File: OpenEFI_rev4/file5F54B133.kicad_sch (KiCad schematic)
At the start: 104 parts, among them J9 Conn_02x06_Top_Bottom, Q14 AO3400A, Q15 AO3400A, Q16 AO3400A, U10 LMV324, U19 f042_wideband_module, U2 74HC4851, U25 TJA1051T-3, U26 SP720ABTG, U8 BMP280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

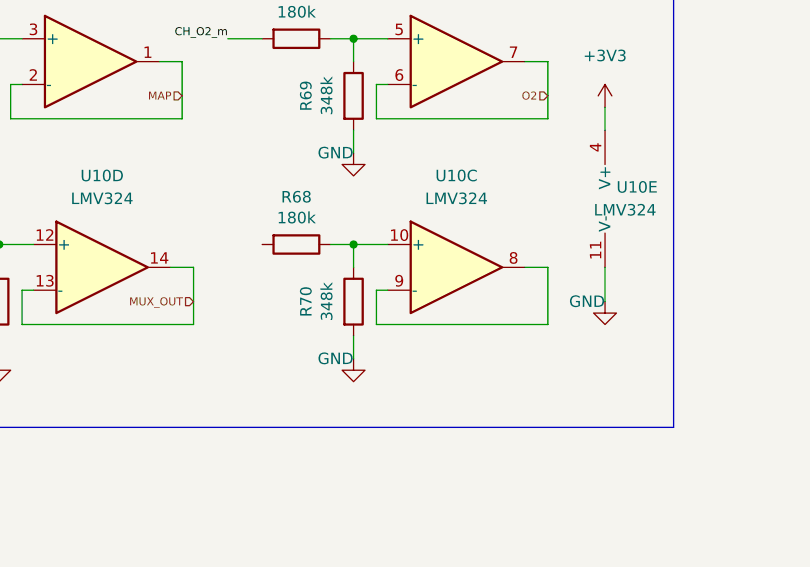
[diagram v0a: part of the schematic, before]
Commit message: update sensors/connector pinout, added rtc vbatt backup
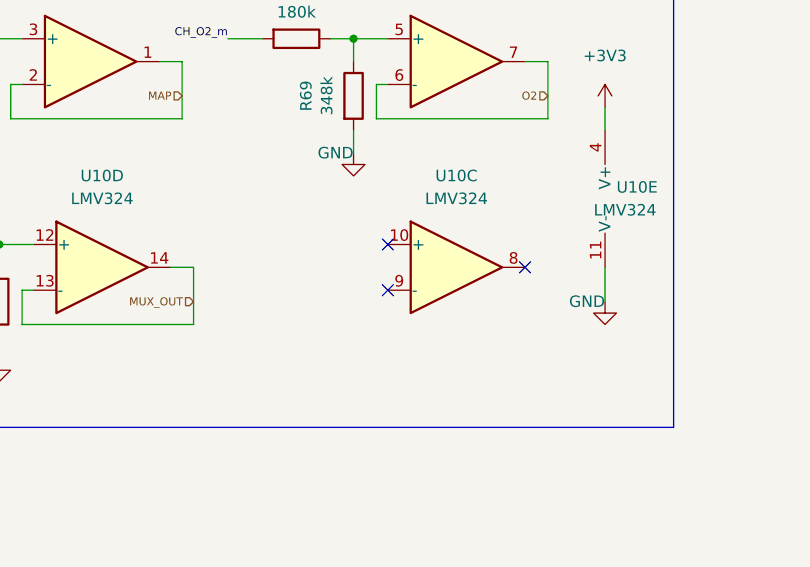
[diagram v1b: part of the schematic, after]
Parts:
- removed R68: 180k, Resistor_SMD:R_0805_2012Metric, symbol Device:R
- removed R70: 348k, Resistor_SMD:R_0805_2012Metric, symbol Device:R
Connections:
- net at U10.8: no longer U10.9 (-)
- no-connect marks 2 -> 5
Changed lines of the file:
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@@
   (junction (at 170.815 90.17) (diameter 0) (color 0 0 0 0)
   )
-  (junction (at 168.91 220.98) (diameter 0) (color 0 0 0 0)
-  )
   (junction (at 74.93 144.78) (diameter 0) (color 0 0 0 0)
   )
@@
   (junction (at 319.405 38.1) (diameter 0) (color 0 0 0 0)
   )
+  (no_connect (at 172.72 226.06))
+  (no_connect (at 172.72 220.98))
   (no_connect (at 300.355 76.2))
   (no_connect (at 313.055 66.04))
+  (no_connect (at 187.96 223.52))
   (wire (pts (xy 171.45 203.2) (xy 171.45 207.01))
     (stroke (width 0) (type default))
@@
     (stroke (width 0) (type default))
   )
-  (wire (pts (xy 171.45 226.06) (xy 171.45 229.87))
-    (stroke (width 0) (type default))
-  )
   (wire (pts (xy 241.3 71.755) (xy 241.3 73.66))
     (stroke (width 0) (type default))
@@
     (stroke (width 0) (type default))
   )
-  (wire (pts (xy 168.91 233.68) (xy 168.91 231.14))
-    (stroke (width 0) (type default))
-  )
   (wire (pts (xy 85.725 223.52) (xy 85.725 226.695))
     (stroke (width 0) (type default))
@@
     (stroke (width 0) (type default))
   )
-  (wire (pts (xy 172.72 226.06) (xy 171.45 226.06))
-    (stroke (width 0) (type default))
-  )
   (polyline (pts (xy 184.785 26.67) (xy 184.785 51.435))
     (stroke (width 0) (type default))
@@
     (stroke (width 0) (type default))
   )
-  (wire (pts (xy 168.91 220.98) (xy 168.91 223.52))
-    (stroke (width 0) (type default))
-  )
   (wire (pts (xy 381 39.37) (xy 390.525 39.37))
     (stroke (width 0) (type default))
@@
     (stroke (width 0) (type default))
   )
-  (wire (pts (xy 190.5 229.87) (xy 190.5 223.52))
-    (stroke (width 0) (type default))
-  )
   (wire (pts (xy 381 41.91) (xy 390.525 41.91))
     (stroke (width 0) (type default))
@@
     (stroke (width 0) (type default))
   )
-  (wire (pts (xy 190.5 223.52) (xy 187.96 223.52))
-    (stroke (width 0) (type default))
-  )
   (wire (pts (xy 114.935 45.72) (xy 118.745 45.72))
     (stroke (width 0) (type default))
@@
     (stroke (width 0) (type default))
   )
-  (wire (pts (xy 168.91 220.98) (xy 172.72 220.98))
-    (stroke (width 0) (type default))
-  )
   (wire (pts (xy 35.56 147.32) (xy 35.56 149.86))
     (stroke (width 0) (type default))
@@
     (stroke (width 0) (type default))
   )
-  (wire (pts (xy 166.37 220.98) (xy 168.91 220.98))
-    (stroke (width 0) (type default))
-  )
   (wire (pts (xy 128.905 48.26) (xy 128.905 45.72))
     (stroke (width 0) (type default))
@@
     (stroke (width 0) (type default))
   )
-  (wire (pts (xy 171.45 229.87) (xy 190.5 229.87))
-    (stroke (width 0) (type default))
-  )
   (polyline (pts (xy 60.96 204.47) (xy 60.96 241.3))
     (stroke (width 0) (type default))
@@
     )
   )
-  (symbol (lib_id "Device:R") (at 162.56 220.98 270) (unit 1)
-    (in_bom yes) (on_board yes) (dnp no)
-    (property "Reference" "R68" (at 162.56 215.7222 90)
-      (effects (font (size 1.27 1.27)))
-    )
-    (property "Value" "180k" (at 162.56 218.0336 90)
-      (effects (font (size 1.27 1.27)))
-    )
-    (property "Footprint" "Resistor_SMD:R_0805_2012Metric" (at 162.56 219.202 90)
-      (effects (font (size 1.27 1.27)) hide)
-    )
-    (property "Datasheet" "~" (at 162.56 220.98 0)
-      (effects (font (size 1.27 1.27)) hide)
-    )
-    (property "Digikey Part Number" "311-180KCRCT-ND" (at 162.56 220.98 0)
-      (effects (font (size 1.27 1.27)) hide)
-    )
-    (property "Manufacturer_Name" "Yageo" (at 162.56 220.98 0)
-      (effects (font (size 1.27 1.27)) hide)
-    )
-    (property "Manufacturer_Part_Number" "RC0805FR-07180KL" (at 162.56 220.98 0)
-      (effects (font (size 1.27 1.27)) hide)
-    )
-    (property "URL" "https://www.digikey.com.au/product-detail/en/yageo/RC0805FR-07180KL/311-180KCRCT-ND/730597" (at 162.56 220.98 0)
-      (effects (font (size 1.27 1.27)) hide)
-    )
-    (pin "1")
-    (pin "2")
-    (instances
-      (project "OpenEFI_rev4"
-        (path "/b282ce4b-c3d0-4c94-b06c-73b92bb672a9/00000000-0000-0000-0000-00005f54b134"
-          (reference "R68") (unit 1)
-        )
-      )
-      (project "DropBear"
-        (path "/ebe274a6-1c43-4fa2-9d2a-7756c5a7217c/00000000-0000-0000-0000-00005cfb00f8"
-          (reference "R46") (unit 1)
-        )
-      )
-    )
-  )
   (symbol (lib_id "power:+5C") (at 46.355 254 0) (unit 1)
     (in_bom yes) (on_board yes) (dnp no)
@@
     )
   )
-  (symbol (lib_id "power:GND") (at 168.91 233.68 0) (unit 1)
-    (in_bom yes) (on_board yes) (dnp no)
-    (property "Reference" "#PWR085" (at 168.91 240.03 0)
-      (effects (font (size 1.27 1.27)) hide)
-    )
-    (property "Value" "GND" (at 168.91 233.68 0)
-      (effects (font (size 1.27 1.27)) (justify right))
-    )
-    (property "Footprint" "" (at 168.91 233.68 0)
-      (effects (font (size 1.27 1.27)) hide)
-    )
-    (property "Datasheet" "" (at 168.91 233.68 0)
-      (effects (font (size 1.27 1.27)) hide)
-    )
-    (pin "1")
-    (instances
-      (project "OpenEFI_rev4"
-        (path "/b282ce4b-c3d0-4c94-b06c-73b92bb672a9/00000000-0000-0000-0000-00005f54b134"
-          (reference "#PWR085") (unit 1)
-        )
-      )
-      (project "DropBear"
-        (path "/ebe274a6-1c43-4fa2-9d2a-7756c5a7217c/00000000-0000-0000-0000-00005cfb00f8"
-          (reference "#PWR0158") (unit 1)
-        )
-      )
-    )
-  )
   (symbol (lib_id "power:+5V") (at 300.99 30.48 0) (unit 1)
     (in_bom yes) (on_board yes) (dnp no)
@@
         )
       )
-    )
-  )
-  (symbol (lib_id "Device:R") (at 168.91 227.33 0) (unit 1)
-    (in_bom yes) (on_board yes) (dnp no)
-    (property "Reference" "R70" (at 163.6522 227.33 90)
-      (effects (font (size 1.27 1.27)))
-    )
-    (property "Value" "348k" (at 165.9636 227.33 90)
-      (effects (font (size 1.27 1.27)))
-    )
-    (property "Footprint" "Resistor_SMD:R_0805_2012Metric" (at 167.132 227.33 90)
-      (effects (font (size 1.27 1.27)) hide)
-    )
-    (property "Datasheet" "~" (at 168.91 227.33 0)
-      (effects (font (size 1.27 1.27)) hide)
-    )
-    (property "Digikey Part Number" "P348KCDKR-ND" (at 168.91 227.33 0)
-      (effects (font (size 1.27 1.27)) hide)
-    )
-    (property "Manufacturer_Name" "Panasonic" (at 168.91 227.33 0)
-      (effects (font (size 1.27 1.27)) hide)
-    )
-    (property "Manufacturer_Part_Number" "ERJ-6ENF3483V" (at 168.91 227.33 0)
-      (effects (font (size 1.27 1.27)) hide)
-    )
-    (property "URL" "https://www.digikey.com.au/product-detail/en/panasonic-electronic-components/ERJ-6ENF3483V/P348KCDKR-ND/576673" (at 168.91 227.33 0)
-      (effects (font (size 1.27 1.27)) hide)
-    )
-    (pin "1")
-    (pin "2")
-    (instances
-      (project "OpenEFI_rev4"
-        (path "/b282ce4b-c3d0-4c94-b06c-73b92bb672a9/00000000-0000-0000-0000-00005f54b134"
-          (reference "R70") (unit 1)
-        )
-      )
-      (project "DropBear"
-        (path "/ebe274a6-1c43-4fa2-9d2a-7756c5a7217c/00000000-0000-0000-0000-00005cfb00f8"
-          (reference "R47") (unit 1)
-        )
-      )

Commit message: WIP Analog frontend
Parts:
- removed J9: Conn_02x06_Top_Bottom, mx120:mx120g-12, symbol Connector_Generic:Conn_02x06_Top_Bottom
- added TP67 (x3): TestPoint, TestPoint:TestPoint_THTPad_1.5x1.5mm_Drill0.7mm, symbol Connector:TestPoint
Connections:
- net CH0 is gone; now on net AUX_CH1_m: U2.13 (CH0)
- net CH1 is gone; now on net AUX_CH2_m: U2.14 (CH1)
- net CH2 is gone; now on net AUX_CH3_m: U2.15 (CH2)
- net CH3 is gone; now on net AUX_CH4_m: U2.12 (CH3)
- net CH4 is gone; now on net AUX_CH5_m: U2.1 (CH4)
- net CH5 is gone; now on net AUX_CH6_m: U2.5 (CH5)
- net CH6 is gone; now on net AUX_CH7_m: U2.2 (CH6)
- net CH7 is gone; now on net AUX_CH8_m: U2.4 (CH7)
- net LSU_Heater+ is gone; now on net +12V: U19.7 (VBatt_Sense)
- net +3V3: now also U25.5 (VIO)
- net +5C: no longer R58.1, R58.1, R58.1, U19.1 (5V), U25.3 (VCC)
- net AUX_CH1: no longer C4.1, R38.1, TP10.1
- net AUX_CH1_m: now also C4.1, R38.1, TP10.1, U26.4 (I4); no longer U26.1 (I1)
- net AUX_CH2: no longer C20.1, R11.1, TP11.1
- net AUX_CH2_m: now also C20.1, R11.1, TP11.1, U26.3 (I3); no longer U26.2 (I2)
- net AUX_CH3: no longer C23.1, R14.1, TP12.1
- net AUX_CH3_m: now also C23.1, R14.1, TP12.1, U26.2 (I2); no longer U26.3 (I3)
- net AUX_CH4: no longer C26.1, R37.1, TP13.1
- net AUX_CH4_m: now also C26.1, R37.1, TP13.1, U26.5 (I5); no longer U26.4 (I4)
- net AUX_CH5: no longer C35.1, R8.1, TP16.1
- net AUX_CH5_m: now also C35.1, R8.1, TP16.1, U26.1 (I1); no longer U26.5 (I5)
- net AUX_CH6: no longer C38.1, R60.1, TP17.1
- net AUX_CH6_m: now also C38.1, R60.1, TP17.1, U26.12 (I11); no longer U26.6 (I6)
- net AUX_CH7: no longer C44.1, R42.1, TP18.1
- net AUX_CH7_m: now also C44.1, R42.1, TP18.1, U26.15 (I14); no longer U26.7 (I7)
- net AUX_CH8: no longer C50.1, R40.1, TP21.1
- net AUX_CH8_m: now also C50.1, R40.1, TP21.1, U26.13 (I12); no longer U26.9 (I8)
- net Boot0: now also TP67.1
- net CH_IAT_m: now also U26.7 (I7); no longer U26.15 (I14)
- net CH_O2_m: now also U26.9 (I8); no longer U26.10 (I9)
- net CH_TPS_m: now also U26.6 (I6); no longer U26.12 (I11)
- net CH_VBATT_m: now also U26.10 (I9); no longer U26.13 (I12)
- net at U19.3 (SEL_1): now also TP67.1
- net at U19.4 (SEL_2): now also TP67.1
- new net +5V: R58.1, R58.1, R58.1, U19.1 (5V), U25.3 (VCC)
- no-connect marks 5 -> 3
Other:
- note removed: "black"
- note removed: "green"
- note removed: "grey"
- note removed: "red"
- note removed: "white"
- note removed: "yellow"

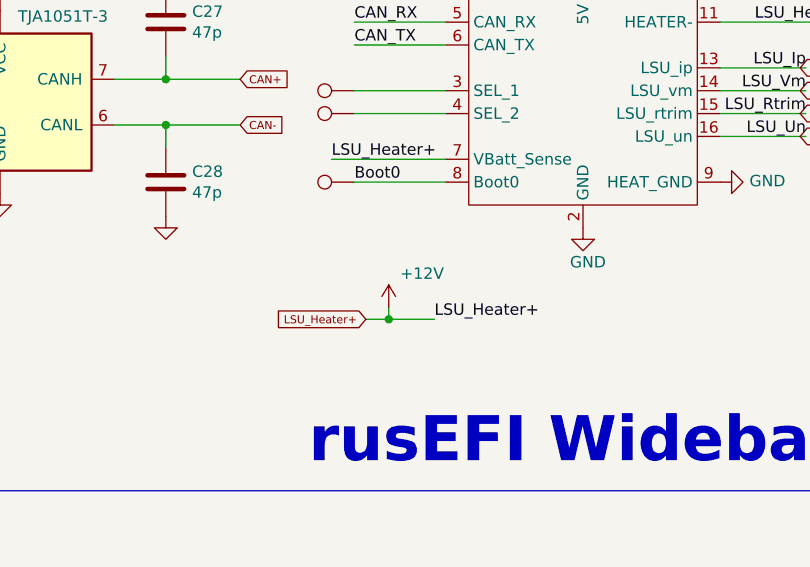
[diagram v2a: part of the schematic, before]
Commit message: fix board errors
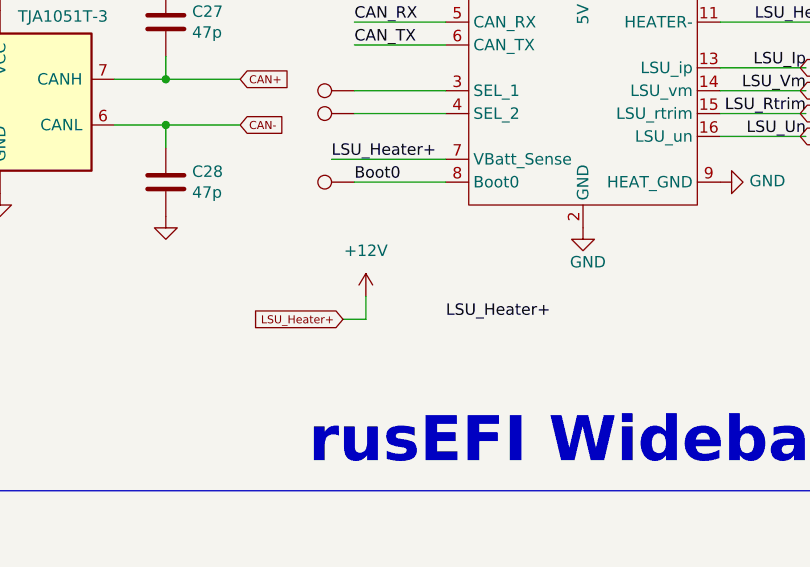
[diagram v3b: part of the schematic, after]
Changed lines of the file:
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@@
   (junction (at 290.83 113.03) (diameter 0) (color 0 0 0 0)
   )
-  (junction (at 344.17 64.77) (diameter 0) (color 0 0 0 0)
-  )
   (junction (at 76.835 144.78) (diameter 0) (color 0 0 0 0)
   )
@@
     (stroke (width 0) (type default))
   )
+  (wire (pts (xy 341.63 62.23) (xy 341.63 64.77))
+    (stroke (width 0) (type default))
+  )
   (wire (pts (xy 76.2 184.15) (xy 76.2 186.69))
     (stroke (width 0) (type default))
@@
     (stroke (width 0) (type default))
   )
+  (wire (pts (xy 341.63 64.77) (xy 339.09 64.77))
+    (stroke (width 0) (type default))
+  )
   (wire (pts (xy 151.13 90.17) (xy 156.845 90.17))
     (stroke (width 0) (type default))
@@
     (stroke (width 0) (type default))
   )
-  (wire (pts (xy 349.25 64.77) (xy 344.17 64.77))
-    (stroke (width 0) (type default))
-  )
   (wire (pts (xy 251.46 83.82) (xy 254 83.82))
     (stroke (width 0) (type default))
@@
     (stroke (width 0) (type default))
   )
-  (wire (pts (xy 344.17 64.77) (xy 344.17 63.5))
-    (stroke (width 0) (type default))
-  )
   (wire (pts (xy 218.44 95.25) (xy 229.87 95.25))
     (stroke (width 0) (type default))
@@
     (stroke (width 0) (type default))
   )
-  (wire (pts (xy 341.63 64.77) (xy 344.17 64.77))
-    (stroke (width 0) (type default))
-  )
   (wire (pts (xy 233.68 53.34) (xy 233.68 55.88))
     (stroke (width 0) (type default))
@@
     (effects (font (size 0.889 0.889)) (justify right bottom))
   )
-  (label "LSU_Heater+" (at 349.25 64.77 0) (fields_autoplaced)
+  (label "LSU_Heater+" (at 350.52 64.77 0) (fields_autoplaced)
     (effects (font (size 1.27 1.27)) (justify left bottom))
   )
@@
     )
   )
-  (global_label "LSU_Heater+" (shape input) (at 341.63 64.77 180)
+  (global_label "LSU_Heater+" (shape input) (at 339.09 64.77 180)
     (effects (font (size 0.889 0.889)) (justify right))
-    (property "Intersheetrefs" "${INTERSHEET_REFS}" (at 338.2053 64.7145 0)
+    (property "Intersheetrefs" "${INTERSHEET_REFS}" (at 335.6653 64.7145 0)
       (effects (font (size 0.889 0.889)) (justify right) hide)
     )
@@
     )
   )
-  (symbol (lib_id "power:+12V") (at 344.17 63.5 0) (unit 1)
-    (in_bom yes) (on_board yes) (dnp no)
-    (property "Reference" "#PWR051" (at 344.17 67.31 0)
-      (effects (font (size 1.27 1.27)) hide)
-    )
-    (property "Value" "+12V" (at 345.44 59.69 0)
-      (effects (font (size 1.27 1.27)) (justify left))
-    )
-    (property "Footprint" "" (at 344.17 63.5 0)
-      (effects (font (size 1.27 1.27)) hide)
-    )
-    (property "Datasheet" "" (at 344.17 63.5 0)
-      (effects (font (size 1.27 1.27)) hide)
-    )
-    (pin "1")
-    (instances
-      (project "OpenEFI_rev4"
-        (path "/b282ce4b-c3d0-4c94-b06c-73b92bb672a9"
-          (reference "#PWR051") (unit 1)
-        )
-        (path "/b282ce4b-c3d0-4c94-b06c-73b92bb672a9/00000000-0000-0000-0000-00005f54b134"
-          (reference "#PWR0180") (unit 1)
-        )
-      )
-    )
-  )
   (symbol (lib_id "Connector:TestPoint_Alt") (at 47.625 86.995 0) (unit 1)
     (in_bom yes) (on_board yes) (dnp no) (fields_autoplaced)
@@
         )
       )
+    )
+  )
+  (symbol (lib_id "power:+12V") (at 341.63 62.23 0) (unit 1)
+    (in_bom yes) (on_board yes) (dnp no) (fields_autoplaced)
+    (property "Reference" "#PWR0180" (at 341.63 66.04 0)
+      (effects (font (size 1.27 1.27)) hide)
+    )
+    (property "Value" "+12V" (at 341.63 57.15 0)
+      (effects (font (size 1.27 1.27)))
+    )
+    (property "Footprint" "" (at 341.63 62.23 0)
+      (effects (font (size 1.27 1.27)) hide)
+    )
+    (property "Datasheet" "" (at 341.63 62.23 0)
+      (effects (font (size 1.27 1.27)) hide)
+    )
+    (pin "1")
+    (instances
+      (project "OpenEFI_rev4"
+        (path "/b282ce4b-c3d0-4c94-b06c-73b92bb672a9/00000000-0000-0000-0000-00005f54b134"
+          (reference "#PWR0180") (unit 1)
+        )
+      )
